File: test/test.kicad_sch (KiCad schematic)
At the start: 3 parts, among them U1 NE555D

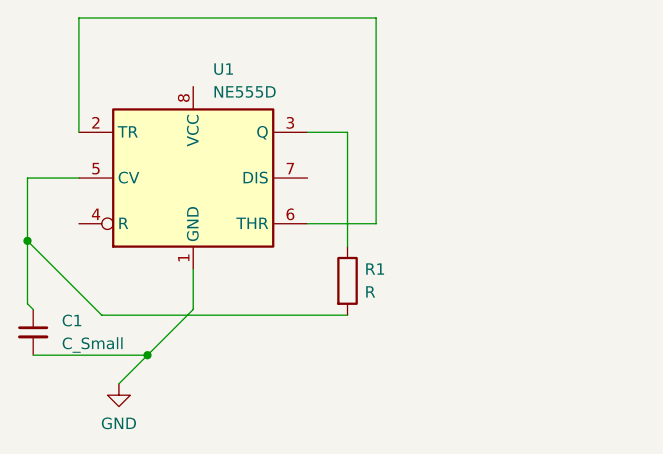
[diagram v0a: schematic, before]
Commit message: adding resistors
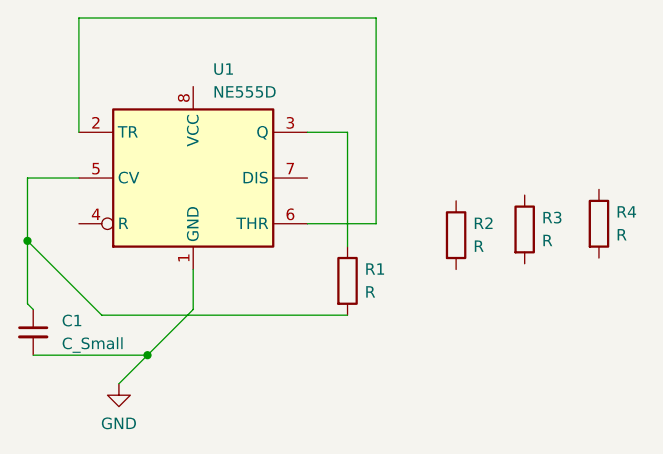
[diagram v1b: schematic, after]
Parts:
- added R2, R3, R4: R, symbol Device:R
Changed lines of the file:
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@@
     (stroke (width 0) (type default))
+  )
+  (symbol (lib_id "Device:R") (at 137.795 77.47 0) (unit 1)
+    (in_bom yes) (on_board yes) (dnp no) (fields_autoplaced)
+    (property "Reference" "R2" (at 139.7 76.2 0)
+      (effects (font (size 1.27 1.27)) (justify left))
+    )
+    (property "Value" "R" (at 139.7 78.74 0)
+      (effects (font (size 1.27 1.27)) (justify left))
+    )
+    (property "Footprint" "" (at 136.017 77.47 90)
+      (effects (font (size 1.27 1.27)) hide)
+    )
+    (property "Datasheet" "~" (at 137.795 77.47 0)
+      (effects (font (size 1.27 1.27)) hide)
+    )
+    (pin "1")
+    (pin "2")
+    (instances
+      (project "test"
+        (path "/bfe11394-a53c-4a06-a363-2abf0fc46245"
+          (reference "R2") (unit 1)
+        )
+      )
+    )
+  )
+  (symbol (lib_id "Device:R") (at 153.67 76.2 0) (unit 1)
+    (in_bom yes) (on_board yes) (dnp no) (fields_autoplaced)
+    (property "Reference" "R4" (at 155.575 74.93 0)
+      (effects (font (size 1.27 1.27)) (justify left))
+    )
+    (property "Value" "R" (at 155.575 77.47 0)
+      (effects (font (size 1.27 1.27)) (justify left))
+    )
+    (property "Footprint" "" (at 151.892 76.2 90)
+      (effects (font (size 1.27 1.27)) hide)
+    )
+    (property "Datasheet" "~" (at 153.67 76.2 0)
+      (effects (font (size 1.27 1.27)) hide)
+    )
+    (pin "1")
+    (pin "2")
+    (instances
+      (project "test"
+        (path "/bfe11394-a53c-4a06-a363-2abf0fc46245"
+          (reference "R4") (unit 1)
+        )
+      )
+    )
   )
   (symbol (lib_id "Device:C_Small") (at 90.805 88.265 0) (unit 1)
@@
         )
       )
+    )
+  )
+  (symbol (lib_id "Device:R") (at 145.415 76.835 0) (unit 1)
+    (in_bom yes) (on_board yes) (dnp no) (fields_autoplaced)
+    (property "Reference" "R3" (at 147.32 75.565 0)
+      (effects (font (size 1.27 1.27)) (justify left))
+    )
+    (property "Value" "R" (at 147.32 78.105 0)
+      (effects (font (size 1.27 1.27)) (justify left))
+    )
+    (property "Footprint" "" (at 143.637 76.835 90)
+      (effects (font (size 1.27 1.27)) hide)
+    )
+    (property "Datasheet" "~" (at 145.415 76.835 0)
+      (effects (font (size 1.27 1.27)) hide)
+    )
+    (pin "1")
+    (pin "2")
+    (instances
+      (project "test"
+        (path "/bfe11394-a53c-4a06-a363-2abf0fc46245"
+          (reference "R3") (unit 1)
+        )
+      )
